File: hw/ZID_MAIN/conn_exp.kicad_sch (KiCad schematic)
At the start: 24 parts, among them J10 USB-C PWR ONLY, J8 BRK EXP SOCKET, J9 Z80-TARGET, U24 74LVC125

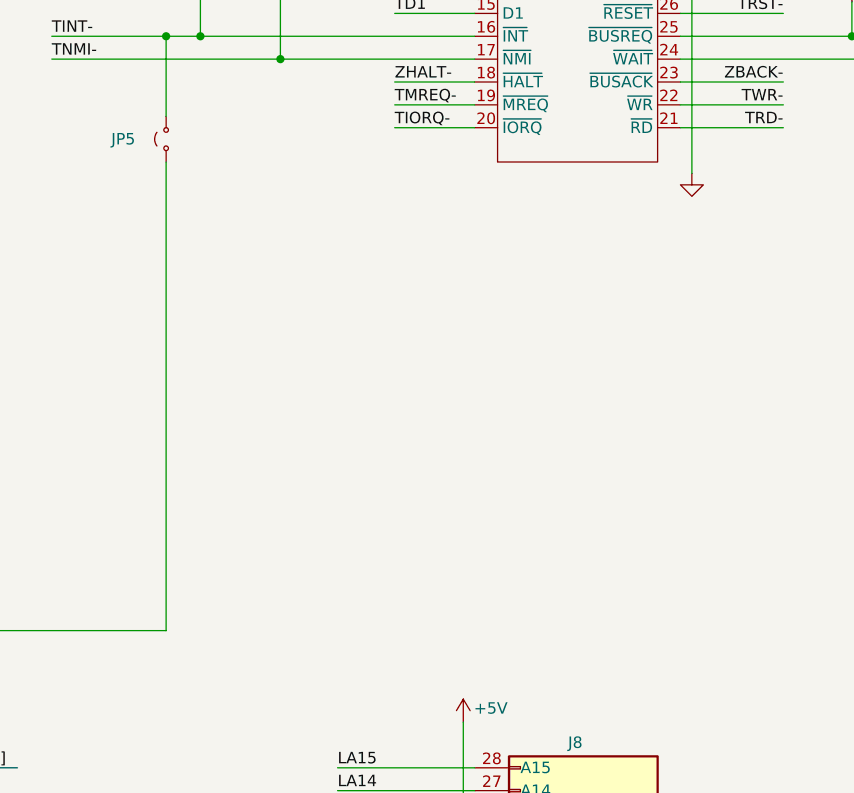
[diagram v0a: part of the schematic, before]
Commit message: Address pull-ups, small updates.
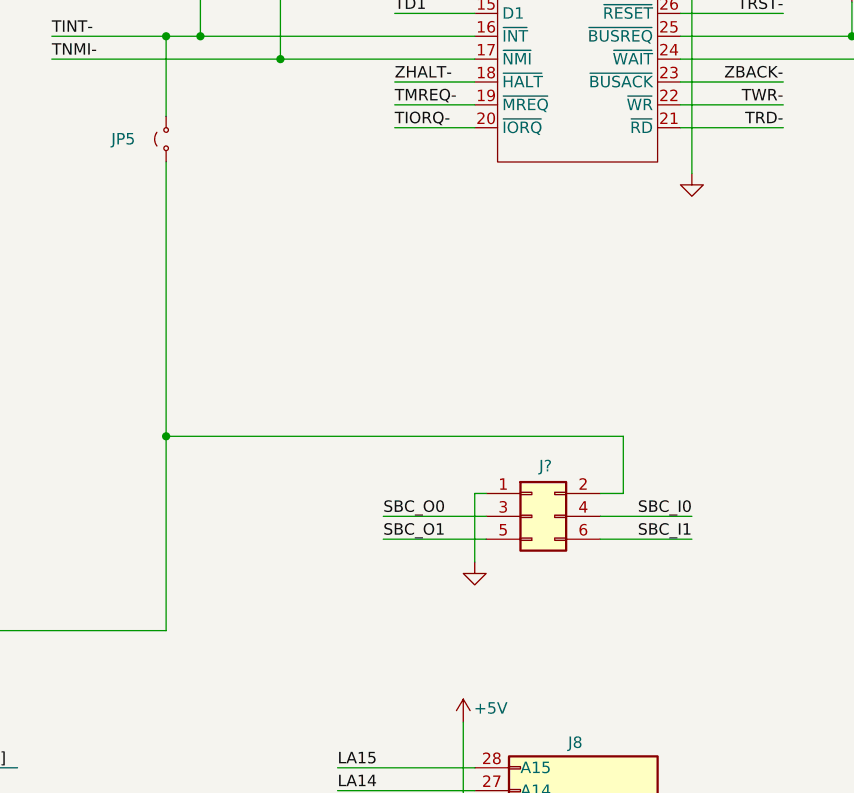
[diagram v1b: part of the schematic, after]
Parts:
- added J?: Conn_02x03_Odd_Even, symbol Connector_Generic:Conn_02x03_Odd_Even
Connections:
- net GND: now also J?.1 (Pin_1)
- net MODINT-: now also J?.2 (Pin_2)
- new net SBC_I0: J?.4 (Pin_4)
- new net SBC_I1: J?.6 (Pin_6)
- new net SBC_O0: J?.3 (Pin_3)
- new net SBC_O1: J?.5 (Pin_5)
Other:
- title: (none) -> Target Pod and Break Expand

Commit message: Add TP for open CPLD pins
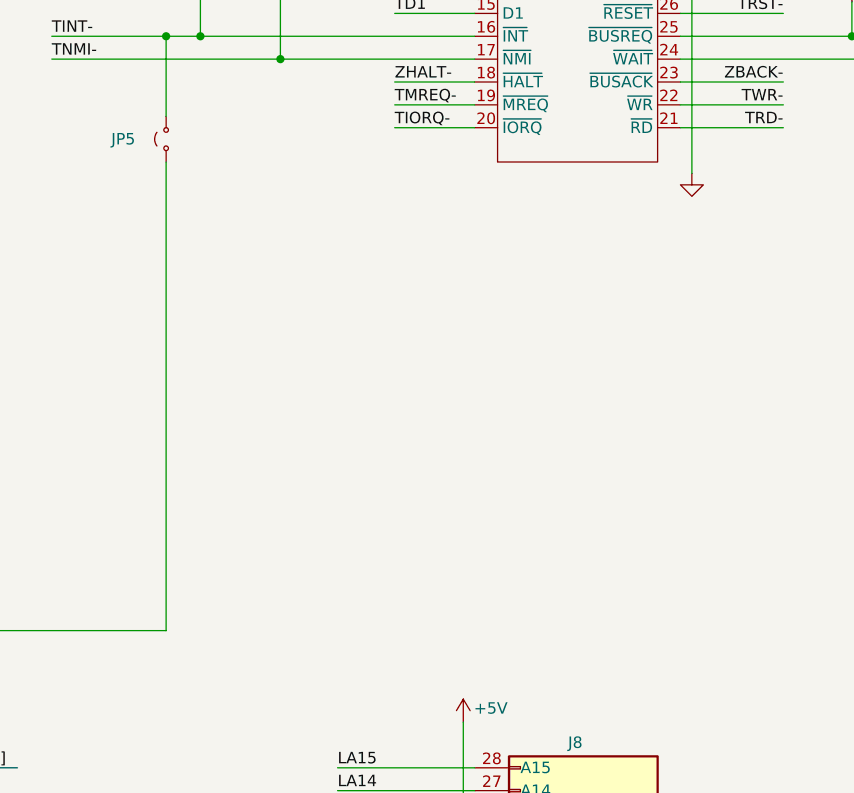
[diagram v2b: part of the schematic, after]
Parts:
- removed J?: Conn_02x03_Odd_Even, symbol Connector_Generic:Conn_02x03_Odd_Even

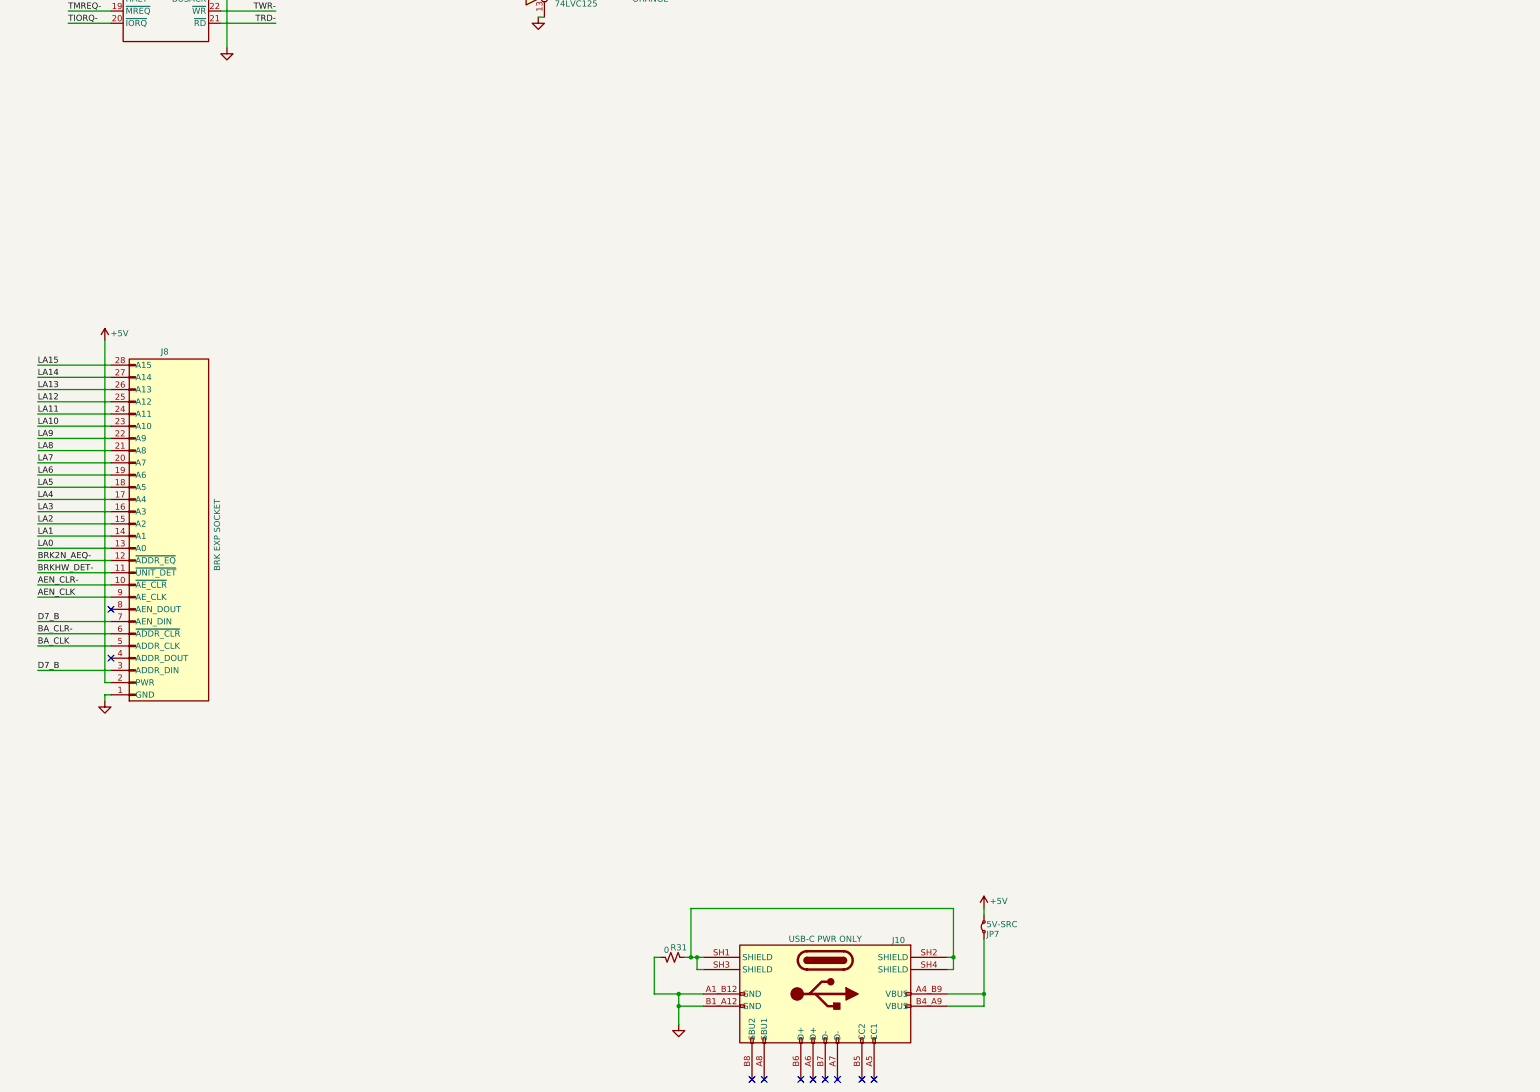
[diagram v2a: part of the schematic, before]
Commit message: 8 output bits on RP. 10k PU for most. TVS.
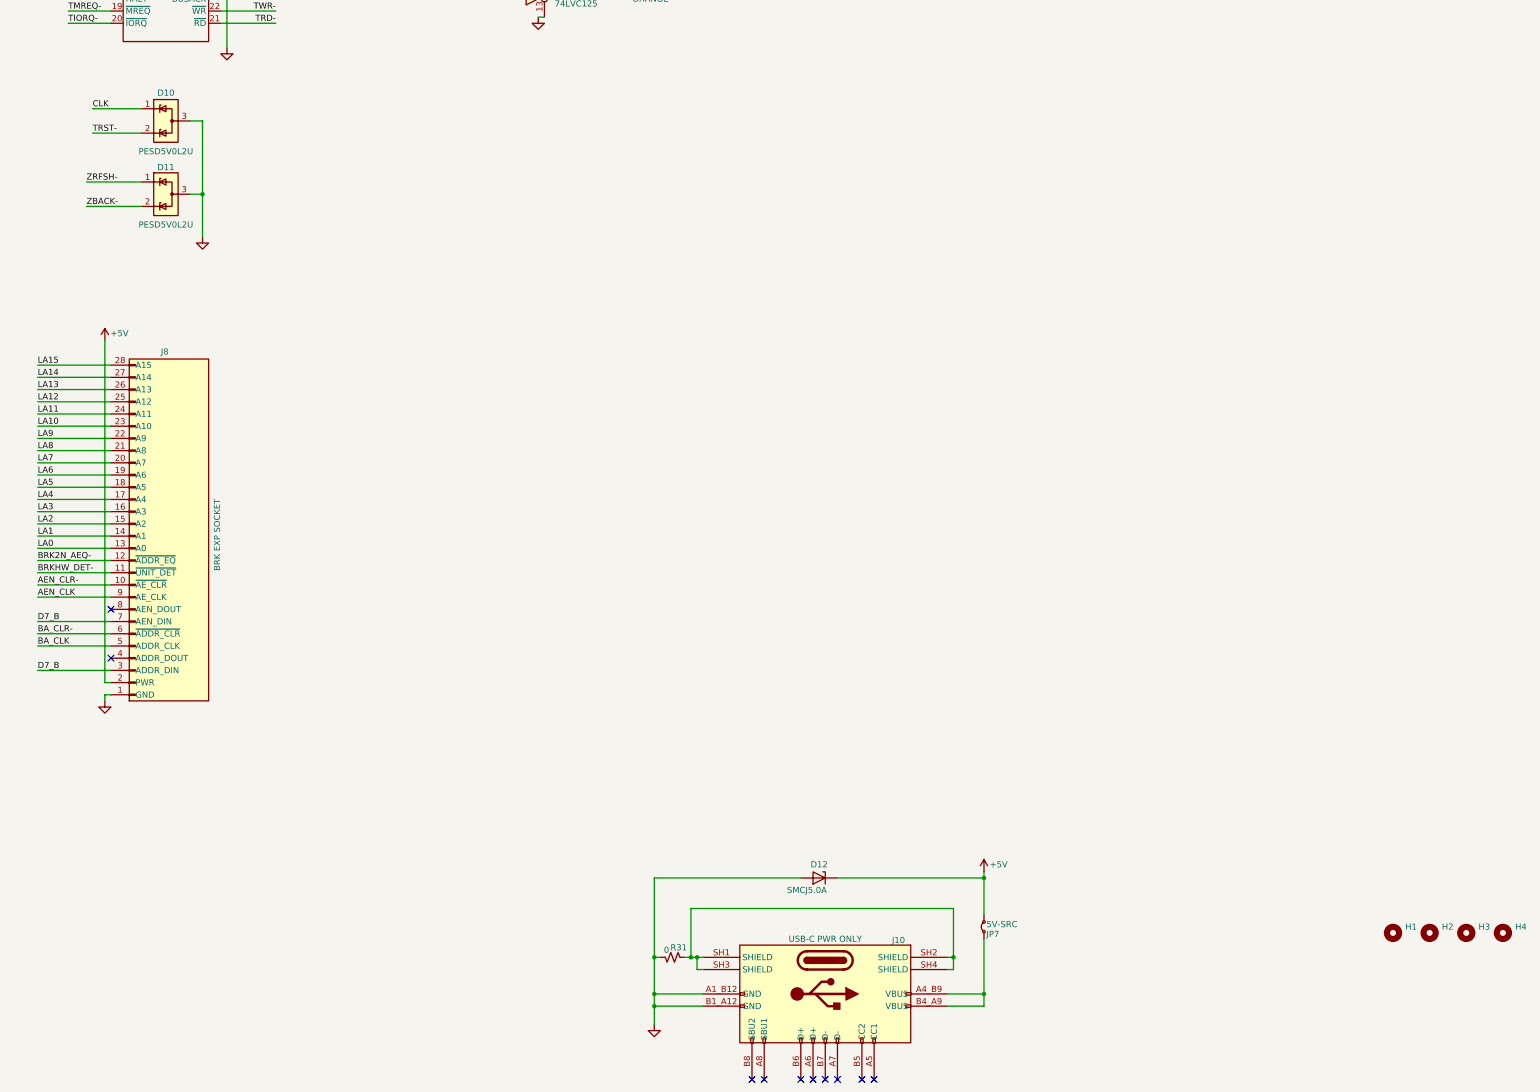
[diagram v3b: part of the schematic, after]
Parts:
- added D10, D11: PESD5V0L2U, Package_TO_SOT_SMD:SOT-23-3, symbol Power_Protection:ESDA5V3L
- added D12: SMCJ5.0A, Diode_SMD:D_SOD-523, symbol Diode:ESD5Zxx
- added H1, H2, H3, H4: MountingHole, symbol Mechanical:MountingHole
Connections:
- net +5V: now also D12.1 (K)
- net CLK: now also D10.1 (K)
- net GND: now also D10.3 (A), D11.3 (A), D12.2 (A)
- net TRST-: now also D10.2 (K)
- net ZBACK-: now also D11.2 (K)
- net ZRFSH-: now also D11.1 (K)
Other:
- company: SilkyDESIGN -> SilkyDESIGN / CMOS1

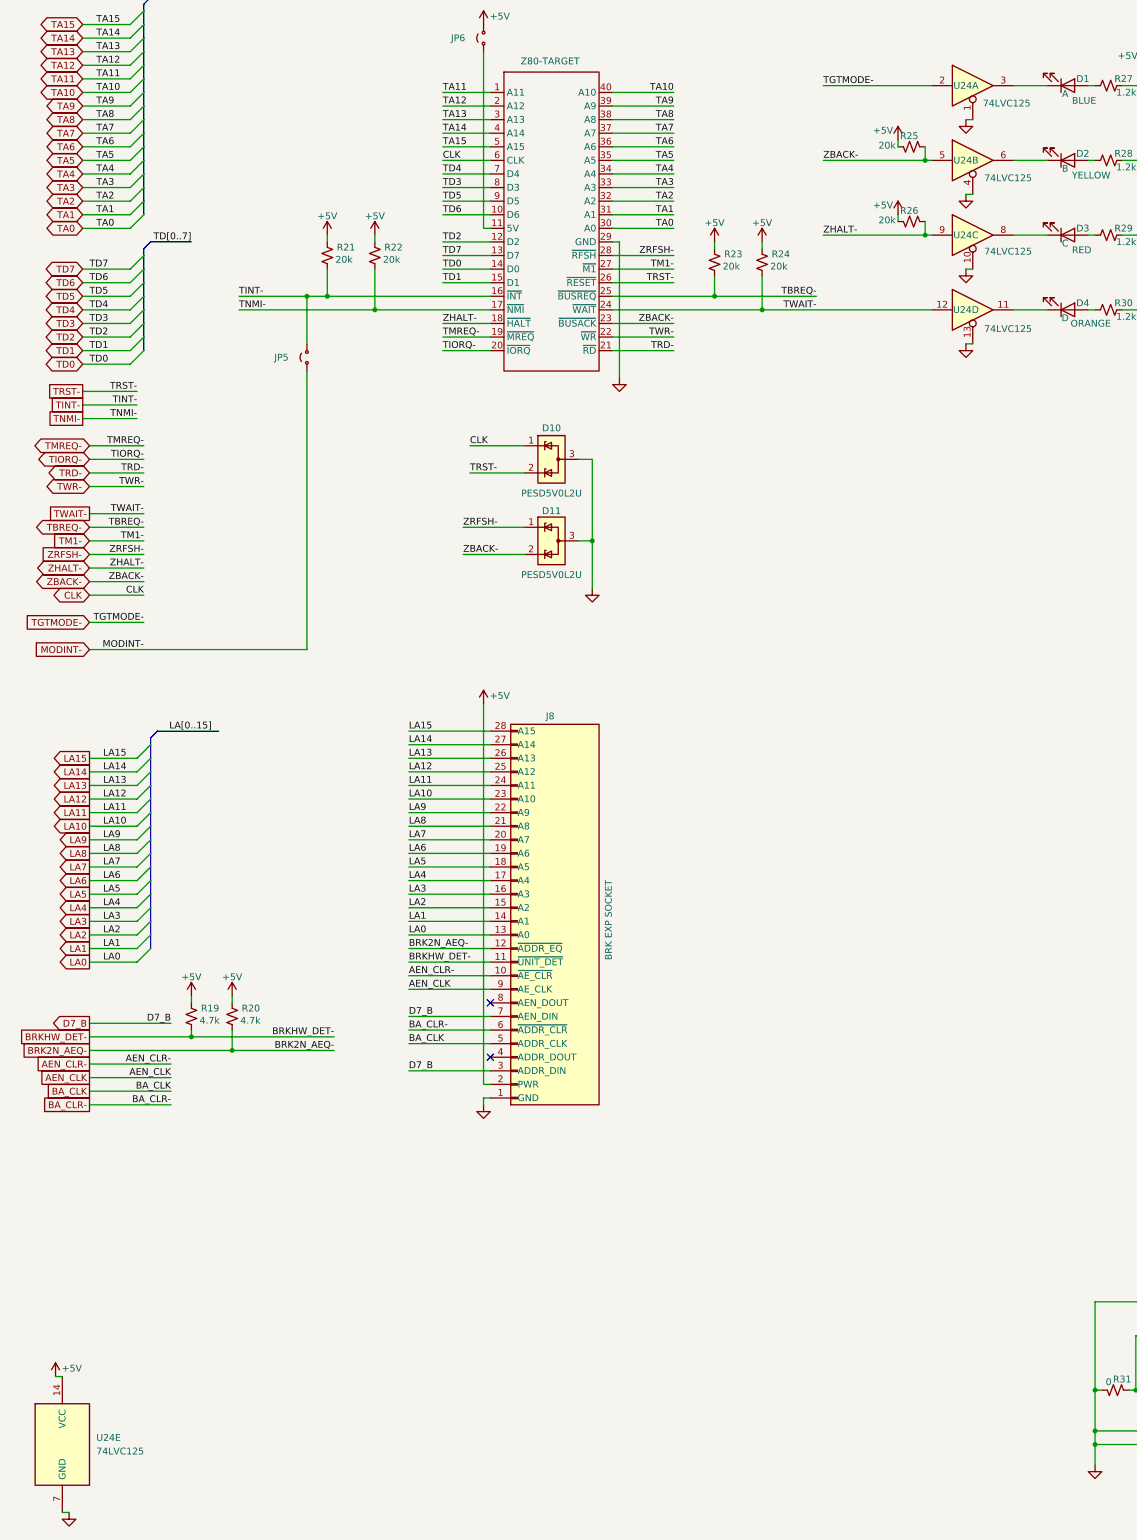
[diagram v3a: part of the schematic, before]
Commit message: U24 from LVC to AHCT for 5V
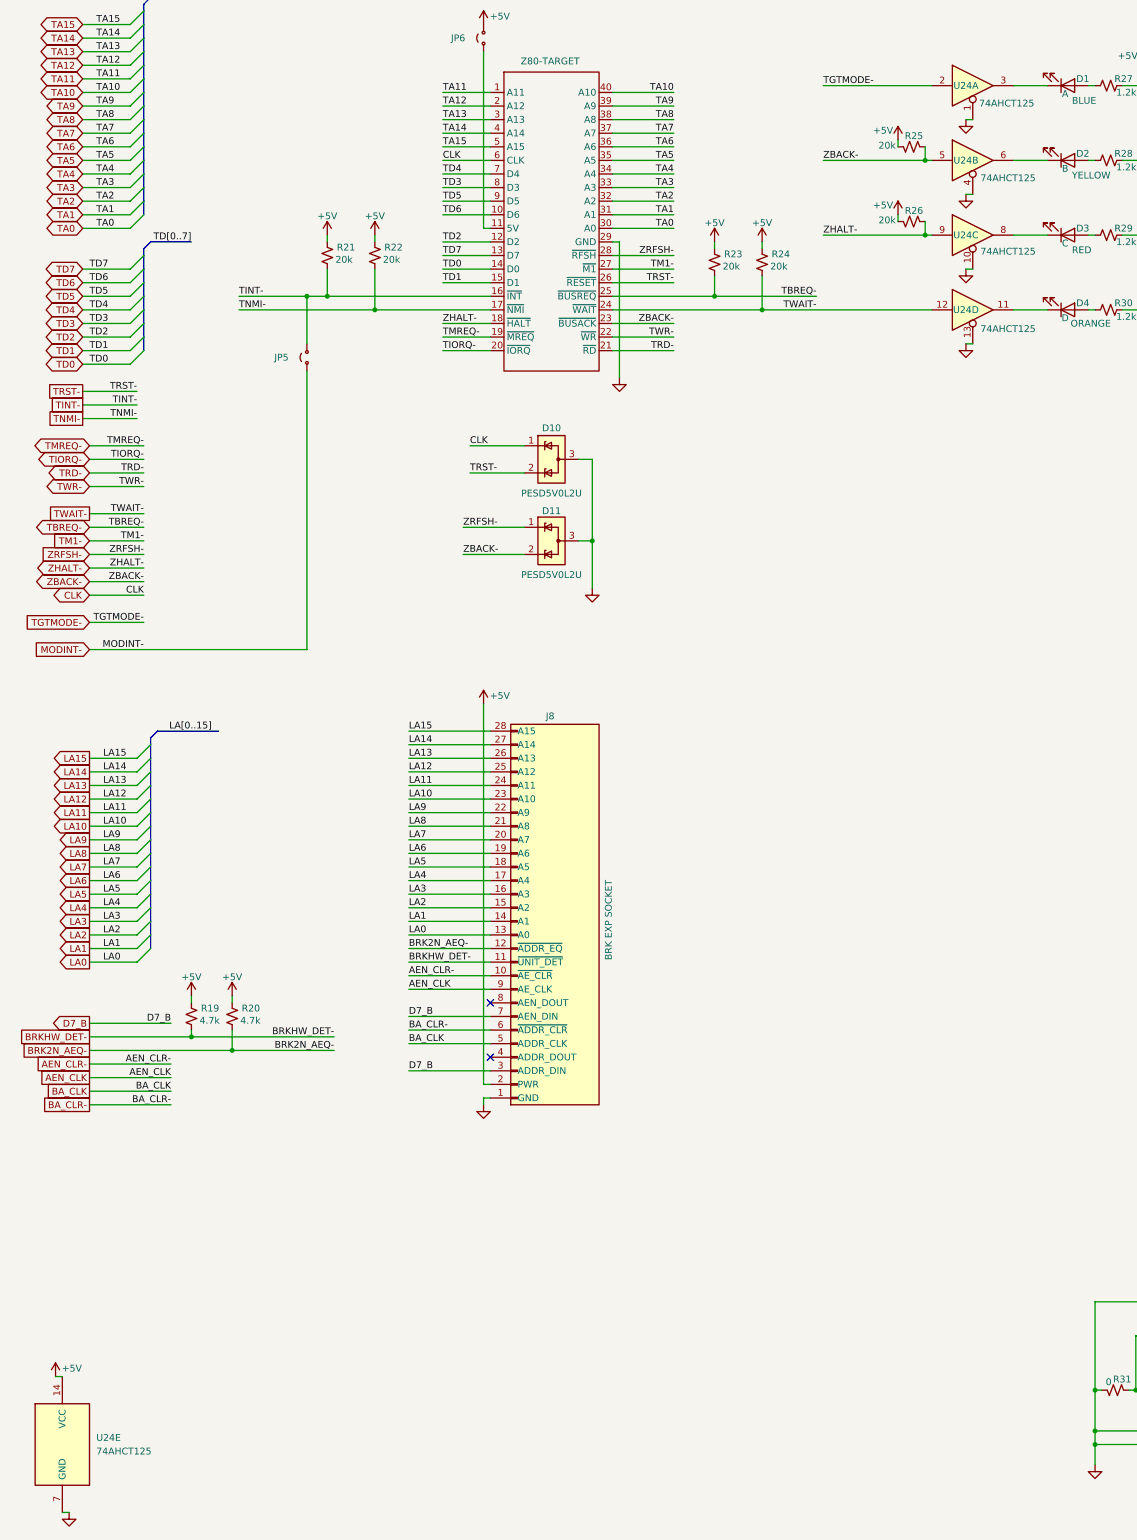
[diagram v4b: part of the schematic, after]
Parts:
- U24: value 74LVC125 -> 74AHCT125
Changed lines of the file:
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@@
 		(dnp no)
 		(property "Reference" "R26"
-			(at 189.23 60.198 90)
+			(at 186.69 60.198 90)
 			(effects
 				(font
 					(size 1.27 1.27)
 				)
-				(justify right)
+				(justify left)
 			)
 		)
@@
 			)
 		)
-		(property "Value" "74LVC125"
+		(property "Value" "74AHCT125"
 			(at 205.994 67.818 0)
 			(effects
@@
 		(dnp no)
 		(property "Reference" "R25"
-			(at 189.23 46.228 90)
+			(at 186.69 46.228 90)
 			(effects
 				(font
 					(size 1.27 1.27)
 				)
-				(justify right)
+				(justify left)
 			)
 		)
@@
 			)
 		)
-		(property "Value" "74LVC125"
+		(property "Value" "74AHCT125"
 			(at 205.74 40.132 0)
 			(effects
@@
 			)
 		)
-		(property "Value" "74LVC125"
+		(property "Value" "74AHCT125"
 			(at 35.56 292.0999 0)
 			(effects
@@
 			)
 		)
-		(property "Value" "74LVC125"
+		(property "Value" "74AHCT125"
 			(at 205.994 82.296 0)
 			(effects
@@
 			)
 		)
-		(property "Value" "74LVC125"
+		(property "Value" "74AHCT125"
 			(at 205.994 54.102 0)
 			(effects
